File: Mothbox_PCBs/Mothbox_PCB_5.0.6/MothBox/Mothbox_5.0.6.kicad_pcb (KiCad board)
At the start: 2 copper layers, 237 x 139 mm, 185 parts, among them J1 DB141V-2.54-4P, J2 DB141V-2.54-4P, J3 DB141V-2.54-4P, J4 DB141V-2.54-4P, J5 Conn_1.25mm, Q1 AP30P30Q, Q10 AP30P30Q, Q13 AP30P30Q, Q2 AO3400A, Q3 YJQ10N2A, Q4 YJQ10N2A, Q5 YJQ10N2A, Q6 YJQ10N2A, Q7 YJQ10N2A, Q8 AP30P30Q, Q9 YJQ10N2A, SW2 KH-6X6X5H-STM, U10 hours_3, U11 Days, U12 MODE, U13 Hours1, U14 Hours2, U15 PCA9555PW, U16 PCA9555PW, U17 DS18B20U, U18 LTR-303ALS-01, U19 graphic, U2 XL4015E1, U3 INA219BIDCNT, U5 RASPBERRY_PI_5, U6 RASPBERRY_PI_4B_4GB, U7 Female Inv Socket Pi 2.54-2*20, U8 GPs 5 pin PM2.54-1*5, U9 PCA9555PW

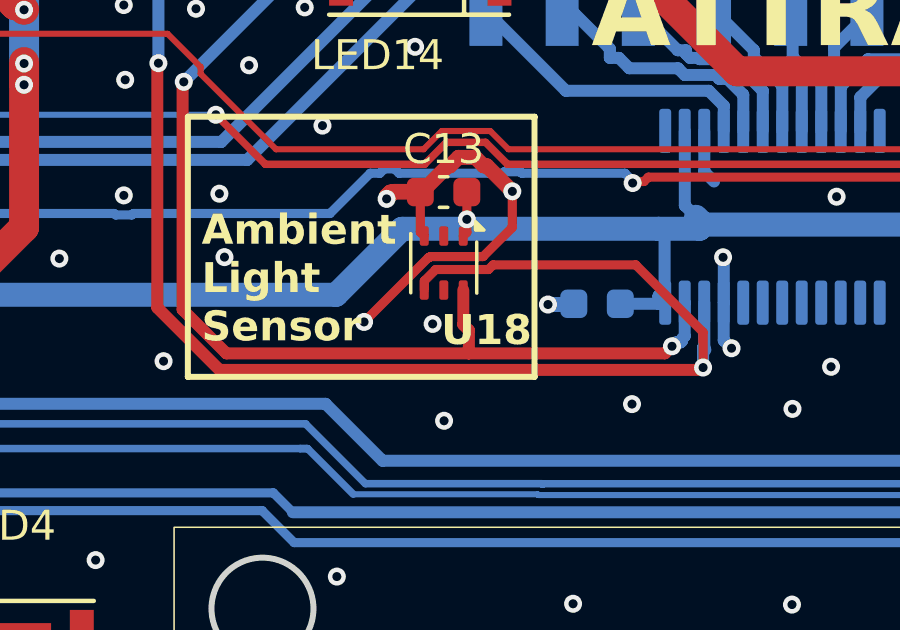
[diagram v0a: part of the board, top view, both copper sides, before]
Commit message: Updated the Light sensor to a more abundant (and low light sensitive) part
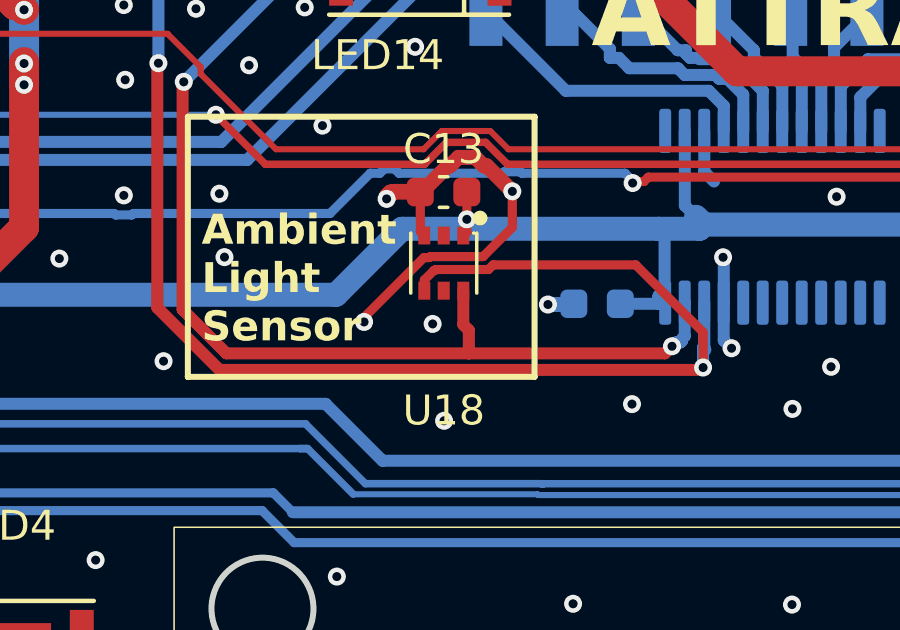
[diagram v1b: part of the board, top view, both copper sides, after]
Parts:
- U18: value LTR-303ALS-01 -> LITEON LTR-F216A; footprint OptoDevice:Lite-On_LTR-303ALS-01 -> EasyEDA:DFN-6_2.0-W2.0_LTR-F216A
- turned U18 to 180 degrees

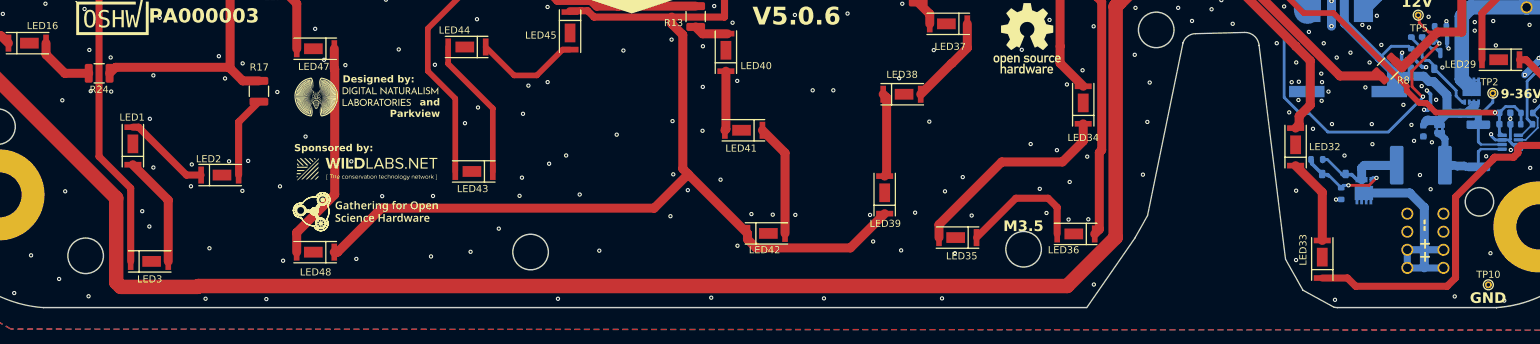
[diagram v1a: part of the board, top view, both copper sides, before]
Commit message: Made a built in switch flipper
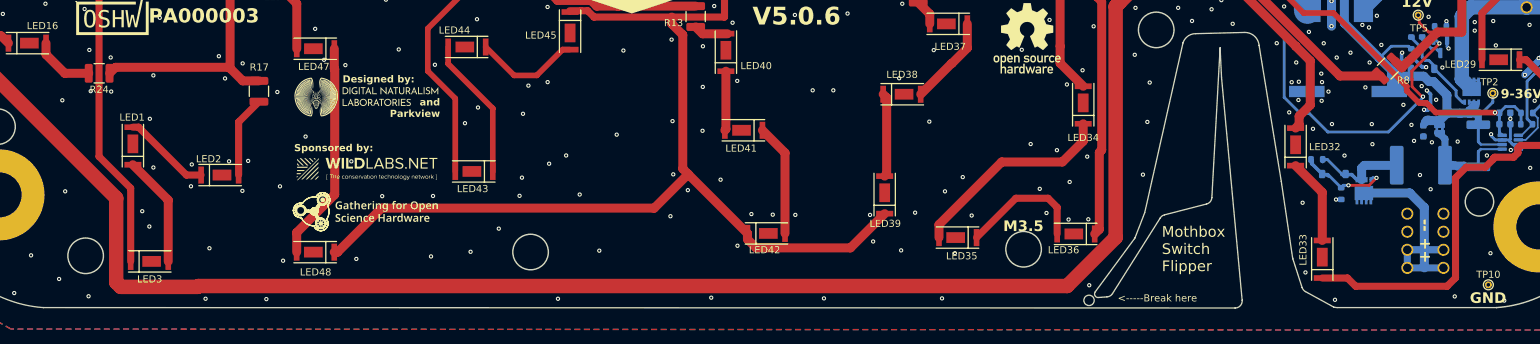
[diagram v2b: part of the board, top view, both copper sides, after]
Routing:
- net Net-(LED27-K): track 487.9 -> 489.5 mm
- net GND: vias 936 -> 937
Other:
- board size 237 x 139 mm -> 237 x 139.1 mm
- board text added: "<-----Break here"
- board text added: "Break here --->"
- board text added: "Mothbox Switch Flipper"
